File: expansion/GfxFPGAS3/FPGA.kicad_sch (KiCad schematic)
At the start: 30 parts, among them J1 JTAG, U301 XC3S500E-4PQG208I, U302 W25Q64JVSSIM, Y1 ECS-3963

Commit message: Latest changes to GfxFPGAS3
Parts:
- D1: footprint (none) -> LED_SMD:LED_1206_3216Metric
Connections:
- net FLASH_D1 is gone; now on net D14: U302.2 (DO/IO1)
- net CLK_25MHZ: now also U301.80 (IP_L10P_2/RDWR_B/GCLK0); no longer U301.103 (IO_L17N_2/CCLK)
- net FLASH_CLK: now also U301.103 (IO_L17N_2/CCLK)
- net HOST_CLK: now also U301.183 (IP_L09P_0/GCLK8); no longer U301.80 (IP_L10P_2/RDWR_B/GCLK0)
- net ~{BUSEN}: now also U301.60 (IO_L03P_2/DOUT/BUSY); no longer U301.55 (IO_L01P_2/CSO_B)
- net ~{DATACS}: now also U301.118 (IP); no longer U301.60 (IO_L03P_2/DOUT/BUSY)
- net ~{REGCS}: now also U301.110 (IP); no longer U301.61 (IO_L03N_2/MOSI/CSI_B)
- net FLASH_CS renamed ~{FLASH_CS}
- net ~{FLASH_CS}: now also U301.55 (IO_L01P_2/CSO_B)
- net FLASH_D0 renamed FLASH_DI
- net FLASH_DI: now also U301.61 (IO_L03N_2/MOSI/CSI_B)
- no-connect marks 21 -> 18
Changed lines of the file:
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@@
   (junction (at 93.98 248.92) (diameter 0) (color 0 0 0 0)
   )
+  (junction (at 234.315 107.95) (diameter 0) (color 0 0 0 0)
+  )
   (junction (at 39.37 218.44) (diameter 0) (color 0 0 0 0)
   )
@@
   (no_connect (at 345.44 154.94))
   (no_connect (at 345.44 152.4))
+  (no_connect (at 58.42 140.97))
   (no_connect (at 345.44 144.78))
   (no_connect (at 58.42 133.35))
   (no_connect (at 58.42 135.89))
-  (no_connect (at 58.42 138.43))
-  (no_connect (at 58.42 140.97))
   (no_connect (at 58.42 147.32))
   (no_connect (at 58.42 149.86))
@@
   (no_connect (at 148.59 153.67))
   (no_connect (at 148.59 151.13))
-  (no_connect (at 148.59 148.59))
-  (no_connect (at 148.59 146.05))
   (no_connect (at 246.38 146.05))
   (wire (pts (xy 337.82 157.48) (xy 345.44 157.48))
@@
     (stroke (width 0) (type default) (color 0 0 0 0))
   )
-  (wire (pts (xy 240.03 64.77) (xy 246.38 64.77))
+  (wire (pts (xy 228.6 64.77) (xy 246.38 64.77))
     (stroke (width 0) (type default) (color 0 0 0 0))
   )
@@
     (stroke (width 0) (type default) (color 0 0 0 0))
   )
+  (wire (pts (xy 51.435 138.43) (xy 58.42 138.43))
+    (stroke (width 0) (type default) (color 0 0 0 0))
+  )
   (wire (pts (xy 266.7 204.47) (xy 270.51 204.47))
     (stroke (width 0) (type default) (color 0 0 0 0))
@@
     (stroke (width 0) (type default) (color 0 0 0 0))
   )
+  (wire (pts (xy 234.315 107.95) (xy 234.315 110.49))
+    (stroke (width 0) (type default) (color 0 0 0 0))
+  )
   (wire (pts (xy 339.09 120.65) (xy 345.44 120.65))
     (stroke (width 0) (type default) (color 0 0 0 0))
@@
     (stroke (width 0) (type default) (color 0 0 0 0))
   )
+  (wire (pts (xy 141.605 148.59) (xy 148.59 148.59))
+    (stroke (width 0) (type default) (color 0 0 0 0))
+  )
   (wire (pts (xy 239.395 140.97) (xy 246.38 140.97))
     (stroke (width 0) (type default) (color 0 0 0 0))
@@
     (stroke (width 0) (type default) (color 0 0 0 0))
   )
+  (wire (pts (xy 232.41 107.95) (xy 234.315 107.95))
+    (stroke (width 0) (type default) (color 0 0 0 0))
+  )
   (wire (pts (xy 246.38 97.79) (xy 240.03 97.79))
     (stroke (width 0) (type default) (color 0 0 0 0))
@@
     (stroke (width 0) (type default) (color 0 0 0 0))
   )
-  (wire (pts (xy 240.03 107.95) (xy 246.38 107.95))
+  (wire (pts (xy 234.315 107.95) (xy 246.38 107.95))
     (stroke (width 0) (type default) (color 0 0 0 0))
   )
@@
     (stroke (width 0) (type default) (color 0 0 0 0))
   )
+  (wire (pts (xy 141.605 146.05) (xy 148.59 146.05))
+    (stroke (width 0) (type default) (color 0 0 0 0))
+  )
   (wire (pts (xy 134.62 212.09) (xy 134.62 209.55))
     (stroke (width 0) (type default) (color 0 0 0 0))
@@
     (stroke (width 0) (type default) (color 0 0 0 0))
   )
-  (wire (pts (xy 240.03 59.69) (xy 246.38 59.69))
+  (wire (pts (xy 228.6 59.69) (xy 246.38 59.69))
     (stroke (width 0) (type default) (color 0 0 0 0))
   )
@@
     (stroke (width 0) (type default) (color 0 0 0 0))
   )
+  (wire (pts (xy 234.315 110.49) (xy 232.41 110.49))
+    (stroke (width 0) (type default) (color 0 0 0 0))
+  )
   (wire (pts (xy 345.44 54.61) (xy 339.09 54.61))
     (stroke (width 0) (type default) (color 0 0 0 0))
@@
     (stroke (width 0) (type default) (color 0 0 0 0))
   )
-  (label "FLASH_CS" (at 132.08 224.79 180)
+  (label "~{FLASH_CS}" (at 132.08 224.79 180)
     (effects (font (size 1.27 1.27)) (justify right bottom))
   )
@@
     (effects (font (size 1.27 1.27)) (justify right bottom))
   )
+  (label "~{FLASH_CS}" (at 240.03 54.61 180)
+    (effects (font (size 1.27 1.27)) (justify right bottom))
+  )
   (label "SRAM_D10" (at 339.09 118.11 180)
     (effects (font (size 1.27 1.27)) (justify right bottom))
@@
     (effects (font (size 1.27 1.27)) (justify right bottom))
   )
+  (label "FLASH_DO" (at 232.41 107.95 180)
+    (effects (font (size 1.27 1.27)) (justify right bottom))
+  )
   (label "FPGA_M2" (at 322.58 186.69 180)
     (effects (font (size 1.27 1.27)) (justify right bottom))
@@
     (effects (font (size 1.27 1.27)) (justify right bottom))
   )
-  (label "FLASH_D0" (at 177.8 229.87 0)
+  (label "FLASH_DI" (at 177.8 229.87 0)
     (effects (font (size 1.27 1.27)) (justify left bottom))
   )
@@
     (effects (font (size 1.27 1.27)) (justify right bottom))
   )
-  (label "FLASH_D1" (at 132.08 227.33 180)
+  (label "FLASH_DO" (at 132.08 227.33 180)
     (effects (font (size 1.27 1.27)) (justify right bottom))
   )
@@
     (effects (font (size 1.27 1.27)) (justify right bottom))
   )
+  (label "FLASH_CLK" (at 240.03 135.89 180)
+    (effects (font (size 1.27 1.27)) (justify right bottom))
+  )
   (label "D11" (at 240.03 115.57 180)
     (effects (font (size 1.27 1.27)) (justify right bottom))
@@
     (effects (font (size 1.27 1.27)) (justify right bottom))
   )
-  (label "D14" (at 240.03 107.95 180)
+  (label "D14" (at 232.41 110.49 180)
     (effects (font (size 1.27 1.27)) (justify right bottom))
   )
@@
     (effects (font (size 1.27 1.27)) (justify right bottom))
   )
-  (label "CLK_25MHZ" (at 240.03 135.89 180)
+  (label "CLK_25MHZ" (at 240.03 156.21 180)
     (effects (font (size 1.27 1.27)) (justify right bottom))
   )
@@
     (effects (font (size 1.27 1.27)) (justify right bottom))
   )
+  (label "FLASH_DI" (at 240.03 67.31 180)
+    (effects (font (size 1.27 1.27)) (justify right bottom))
+  )
   (label "SRAM_A13" (at 52.07 57.15 180)
     (effects (font (size 1.27 1.27)) (justify right bottom))
@@
     (effects (font (size 1.27 1.27)) (justify right))
   )
-  (hierarchical_label "~{REGCS}" (shape input) (at 240.03 67.31 180)
+  (hierarchical_label "~{REGCS}" (shape input) (at 141.605 146.05 180)
     (effects (font (size 1.27 1.27)) (justify right))
   )
@@
     (effects (font (size 1.27 1.27)) (justify right))
   )
-  (hierarchical_label "~{BUSEN}" (shape output) (at 240.03 54.61 180)
+  (hierarchical_label "~{BUSEN}" (shape output) (at 228.6 64.77 180)
     (effects (font (size 1.27 1.27)) (justify right))
   )
@@
     (effects (font (size 1.27 1.27)) (justify right))
   )
-  (hierarchical_label "~{DATACS}" (shape input) (at 240.03 64.77 180)
+  (hierarchical_label "~{DATACS}" (shape input) (at 141.605 148.59 180)
     (effects (font (size 1.27 1.27)) (justify right))
   )
@@
     (effects (font (size 1.27 1.27)) (justify left))
   )
-  (hierarchical_label "HOST_CLK" (shape input) (at 240.03 156.21 180)
+  (hierarchical_label "HOST_CLK" (shape input) (at 51.435 138.43 180)
     (effects (font (size 1.27 1.27)) (justify right))
   )
@@
     (effects (font (size 1.27 1.27)) (justify left))
   )
-  (hierarchical_label "~{RESET}" (shape input) (at 240.03 59.69 180)
+  (hierarchical_label "~{RESET}" (shape input) (at 228.6 59.69 180)
     (effects (font (size 1.27 1.27)) (justify right))
   )
@@
       (effects (font (size 1.27 1.27)) (justify right))
     )
-    (property "Footprint" "" (id 2) (at 332.74 247.65 0)
+    (property "Footprint" "LED_SMD:LED_1206_3216Metric" (id 2) (at 332.74 247.65 0)
       (effects (font (size 1.27 1.27)) hide)
     )

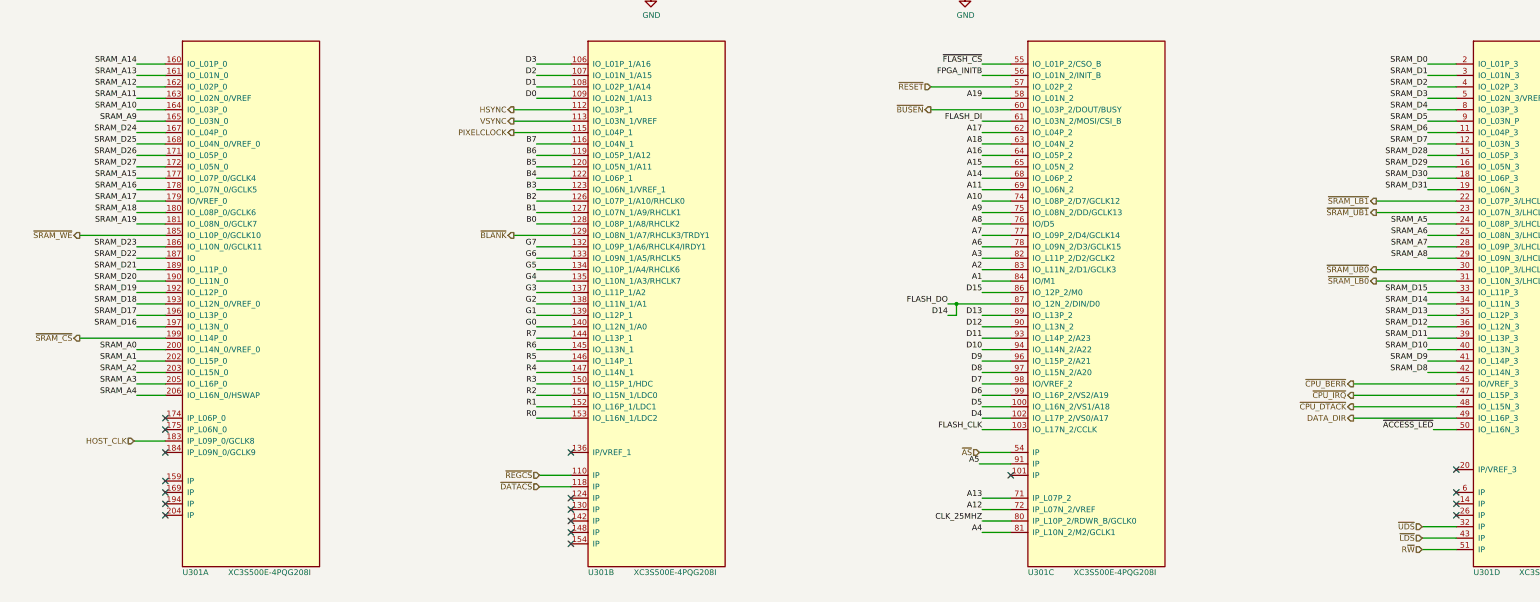
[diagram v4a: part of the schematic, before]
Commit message: Reworking FPGA VGA Card Pinout
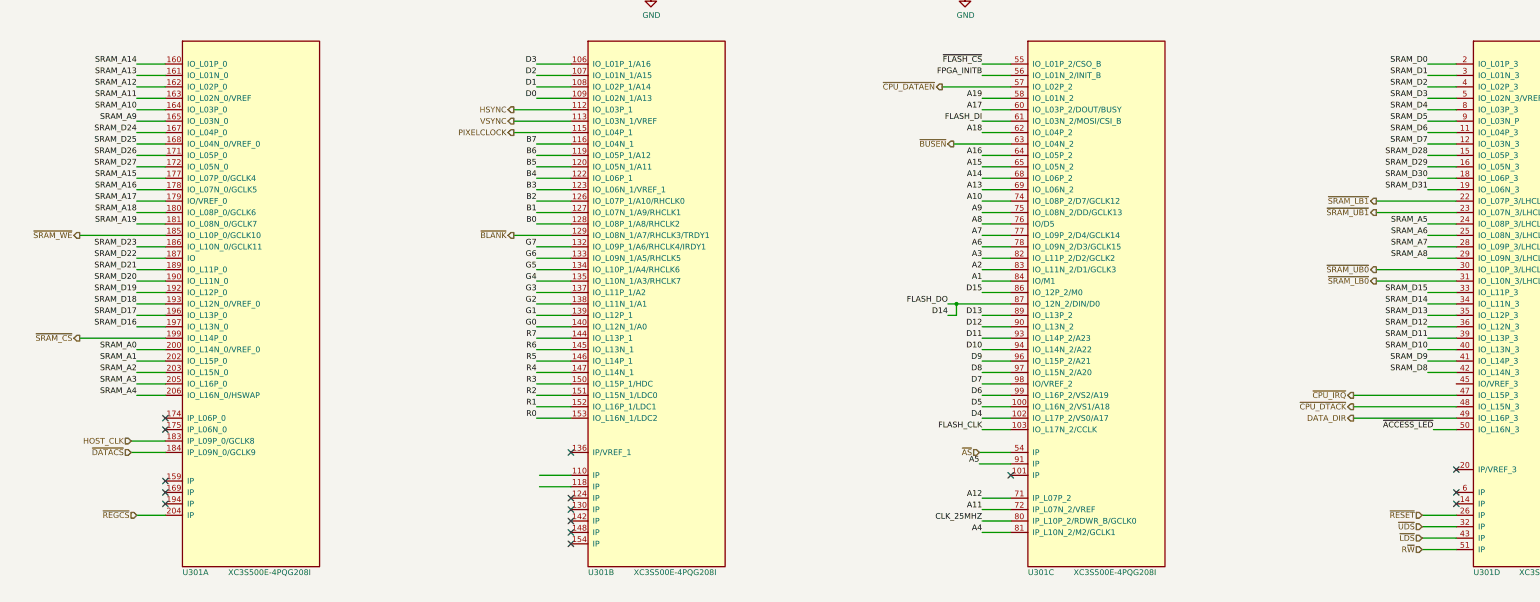
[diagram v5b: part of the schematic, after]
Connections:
- net A11: now also U301.72 (IP_L07N_2/VREF); no longer U301.69 (IO_L06N_2)
- net A12: now also U301.71 (IP_L07P_2); no longer U301.72 (IP_L07N_2/VREF)
- net A13: now also U301.69 (IO_L06N_2); no longer U301.71 (IP_L07P_2)
- net A17: now also U301.60 (IO_L03P_2/DOUT/BUSY); no longer U301.62 (IO_L04P_2)
- net A18: now also U301.62 (IO_L04P_2); no longer U301.63 (IO_L04N_2)
- net ~{BUSEN}: now also U301.63 (IO_L04N_2); no longer U301.60 (IO_L03P_2/DOUT/BUSY)
- net ~{DATACS}: now also U301.184 (IP_L09N_0/GCLK9); no longer U301.118 (IP)
- net ~{REGCS}: now also U301.204 (IP); no longer U301.110 (IP)
- net ~{RESET}: now also U301.26 (IP); no longer U301.57 (IO_L02P_2)
- net ~{CPU_BERR}: no longer names the net of U301.45 (IO/VREF_3)
- new net ~{CPU_DATAEN}: U301.57 (IO_L02P_2)
- no-connect marks 18 -> 15
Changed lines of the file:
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@@
   )
   (no_connect (at 345.44 149.86))
-  (no_connect (at 345.44 154.94))
   (no_connect (at 345.44 152.4))
-  (no_connect (at 58.42 140.97))
   (no_connect (at 345.44 144.78))
   (no_connect (at 58.42 133.35))
@@
   (no_connect (at 58.42 149.86))
   (no_connect (at 58.42 152.4))
-  (no_connect (at 58.42 154.94))
   (no_connect (at 148.59 140.97))
   (no_connect (at 148.59 161.29))
@@
     (stroke (width 0) (type default) (color 0 0 0 0))
   )
+  (wire (pts (xy 231.14 59.69) (xy 246.38 59.69))
+    (stroke (width 0) (type default) (color 0 0 0 0))
+  )
   (wire (pts (xy 203.2 36.83) (xy 215.9 36.83))
     (stroke (width 0) (type default) (color 0 0 0 0))
@@
     (stroke (width 0) (type default) (color 0 0 0 0))
   )
-  (wire (pts (xy 228.6 64.77) (xy 246.38 64.77))
-    (stroke (width 0) (type default) (color 0 0 0 0))
-  )
   (wire (pts (xy 246.38 102.87) (xy 240.03 102.87))
     (stroke (width 0) (type default) (color 0 0 0 0))
@@
     (stroke (width 0) (type default) (color 0 0 0 0))
   )
-  (wire (pts (xy 322.58 125.73) (xy 345.44 125.73))
-    (stroke (width 0) (type default) (color 0 0 0 0))
-  )
   (wire (pts (xy 270.51 251.46) (xy 270.51 252.73))
     (stroke (width 0) (type default) (color 0 0 0 0))
@@
     (stroke (width 0) (type default) (color 0 0 0 0))
   )
-  (wire (pts (xy 51.435 138.43) (xy 58.42 138.43))
-    (stroke (width 0) (type default) (color 0 0 0 0))
-  )
   (wire (pts (xy 266.7 204.47) (xy 270.51 204.47))
     (stroke (width 0) (type default) (color 0 0 0 0))
@@
     (stroke (width 0) (type default) (color 0 0 0 0))
   )
+  (wire (pts (xy 240.03 64.77) (xy 246.38 64.77))
+    (stroke (width 0) (type default) (color 0 0 0 0))
+  )
   (wire (pts (xy 242.57 36.83) (xy 255.27 36.83))
     (stroke (width 0) (type default) (color 0 0 0 0))
@@
     (stroke (width 0) (type default) (color 0 0 0 0))
   )
-  (wire (pts (xy 246.38 72.39) (xy 240.03 72.39))
+  (wire (pts (xy 233.68 72.39) (xy 246.38 72.39))
     (stroke (width 0) (type default) (color 0 0 0 0))
   )
@@
     (stroke (width 0) (type default) (color 0 0 0 0))
   )
+  (wire (pts (xy 50.8 140.97) (xy 58.42 140.97))
+    (stroke (width 0) (type default) (color 0 0 0 0))
+  )
   (wire (pts (xy 246.38 151.13) (xy 240.03 151.13))
     (stroke (width 0) (type default) (color 0 0 0 0))
@@
     (stroke (width 0) (type default) (color 0 0 0 0))
   )
+  (wire (pts (xy 50.8 138.43) (xy 58.42 138.43))
+    (stroke (width 0) (type default) (color 0 0 0 0))
+  )
   (wire (pts (xy 52.07 72.39) (xy 58.42 72.39))
     (stroke (width 0) (type default) (color 0 0 0 0))
@@
     (stroke (width 0) (type default) (color 0 0 0 0))
   )
+  (wire (pts (xy 337.82 154.94) (xy 345.44 154.94))
+    (stroke (width 0) (type default) (color 0 0 0 0))
+  )
   (bus (pts (xy 173.99 271.78) (xy 179.07 271.78))
     (stroke (width 0) (type default) (color 0 0 0 0))
@@
     (stroke (width 0) (type default) (color 0 0 0 0))
   )
-  (wire (pts (xy 228.6 59.69) (xy 246.38 59.69))
-    (stroke (width 0) (type default) (color 0 0 0 0))
-  )
   (wire (pts (xy 223.52 228.6) (xy 223.52 231.14))
     (stroke (width 0) (type default) (color 0 0 0 0))
@@
     (stroke (width 0) (type default) (color 0 0 0 0))
   )
+  (wire (pts (xy 52.07 154.94) (xy 58.42 154.94))
+    (stroke (width 0) (type default) (color 0 0 0 0))
+  )
   (wire (pts (xy 52.07 80.01) (xy 58.42 80.01))
     (stroke (width 0) (type default) (color 0 0 0 0))
@@
     (effects (font (size 1.27 1.27)) (justify right bottom))
   )
-  (label "A13" (at 240.03 151.13 180)
+  (label "A13" (at 240.03 82.55 180)
     (effects (font (size 1.27 1.27)) (justify right bottom))
   )
@@
     (effects (font (size 1.27 1.27)) (justify right bottom))
   )
-  (label "A18" (at 240.03 72.39 180)
+  (label "A18" (at 240.03 69.85 180)
     (effects (font (size 1.27 1.27)) (justify right bottom))
   )
@@
     (effects (font (size 1.27 1.27)) (justify right bottom))
   )
-  (label "A12" (at 240.03 153.67 180)
+  (label "A12" (at 240.03 151.13 180)
     (effects (font (size 1.27 1.27)) (justify right bottom))
   )
@@
     (effects (font (size 1.27 1.27)) (justify right bottom))
   )
-  (label "A17" (at 240.03 69.85 180)
+  (label "A17" (at 240.03 64.77 180)
     (effects (font (size 1.27 1.27)) (justify right bottom))
   )
@@
     (effects (font (size 1.27 1.27)) (justify right bottom))
   )
-  (label "A11" (at 240.03 82.55 180)
+  (label "A11" (at 240.03 153.67 180)
     (effects (font (size 1.27 1.27)) (justify right bottom))
   )
@@
     (effects (font (size 1.27 1.27)) (justify right))
   )
-  (hierarchical_label "~{REGCS}" (shape input) (at 141.605 146.05 180)
+  (hierarchical_label "~{REGCS}" (shape input) (at 52.07 154.94 180)
     (effects (font (size 1.27 1.27)) (justify right))
   )
   (hierarchical_label "VSYNC" (shape output) (at 135.89 67.31 180)
+    (effects (font (size 1.27 1.27)) (justify right))
+  )
+  (hierarchical_label "~{CPU_DATAEN}" (shape output) (at 231.14 59.69 180)
     (effects (font (size 1.27 1.27)) (justify right))
   )
@@
     (effects (font (size 1.27 1.27)) (justify right))
   )
-  (hierarchical_label "~{BUSEN}" (shape output) (at 228.6 64.77 180)
+  (hierarchical_label "~{BUSEN}" (shape output) (at 233.68 72.39 180)
     (effects (font (size 1.27 1.27)) (justify right))
   )
@@
     (effects (font (size 1.27 1.27)) (justify right))
   )
-  (hierarchical_label "~{DATACS}" (shape input) (at 141.605 148.59 180)
+  (hierarchical_label "~{DATACS}" (shape input) (at 50.8 140.97 180)
     (effects (font (size 1.27 1.27)) (justify right))
   )
@@
     (effects (font (size 1.27 1.27)) (justify left))
   )
-  (hierarchical_label "HOST_CLK" (shape input) (at 51.435 138.43 180)
+  (hierarchical_label "HOST_CLK" (shape input) (at 50.8 138.43 180)
     (effects (font (size 1.27 1.27)) (justify right))
   )
@@
     (effects (font (size 1.27 1.27)) (justify left))
   )
-  (hierarchical_label "~{RESET}" (shape input) (at 228.6 59.69 180)
+  (hierarchical_label "~{RESET}" (shape input) (at 337.82 154.94 180)
     (effects (font (size 1.27 1.27)) (justify right))
   )
@@
     (effects (font (size 1.27 1.27)) (justify right))
   )
-  (hierarchical_label "~{CPU_BERR}" (shape output) (at 322.58 125.73 180)
-    (effects (font (size 1.27 1.27)) (justify right))
-  )

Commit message: Fix for BUSENABLE not placable on FPGA
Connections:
- net ~{CPU_DATAEN}: now also U301.45 (IO/VREF_3); no longer U301.57 (IO_L02P_2)
- no-connect marks 15 -> 18
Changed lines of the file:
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@@
   (junction (at 158.75 209.55) (diameter 0) (color 0 0 0 0)
   )
+  (no_connect (at 148.59 146.05))
+  (no_connect (at 148.59 148.59))
+  (no_connect (at 246.38 59.69))
   (no_connect (at 345.44 149.86))
   (no_connect (at 345.44 152.4))
@@
     (stroke (width 0) (type default) (color 0 0 0 0))
   )
-  (wire (pts (xy 231.14 59.69) (xy 246.38 59.69))
-    (stroke (width 0) (type default) (color 0 0 0 0))
-  )
   (wire (pts (xy 203.2 36.83) (xy 215.9 36.83))
     (stroke (width 0) (type default) (color 0 0 0 0))
@@
     (stroke (width 0) (type default) (color 0 0 0 0))
   )
+  (wire (pts (xy 322.58 125.73) (xy 345.44 125.73))
+    (stroke (width 0) (type default) (color 0 0 0 0))
+  )
   (wire (pts (xy 327.66 102.87) (xy 345.44 102.87))
     (stroke (width 0) (type default) (color 0 0 0 0))
@@
     (stroke (width 0) (type default) (color 0 0 0 0))
   )
-  (wire (pts (xy 141.605 148.59) (xy 148.59 148.59))
-    (stroke (width 0) (type default) (color 0 0 0 0))
-  )
   (wire (pts (xy 239.395 140.97) (xy 246.38 140.97))
     (stroke (width 0) (type default) (color 0 0 0 0))
@@
   )
   (wire (pts (xy 236.22 21.59) (xy 236.22 24.13))
-    (stroke (width 0) (type default) (color 0 0 0 0))
-  )
-  (wire (pts (xy 141.605 146.05) (xy 148.59 146.05))
     (stroke (width 0) (type default) (color 0 0 0 0))
   )
@@
     (effects (font (size 1.27 1.27)) (justify right))
   )
-  (hierarchical_label "~{CPU_DATAEN}" (shape output) (at 231.14 59.69 180)
+  (hierarchical_label "~{CPU_DATAEN}" (shape output) (at 322.58 125.73 180)
     (effects (font (size 1.27 1.27)) (justify right))
   )
